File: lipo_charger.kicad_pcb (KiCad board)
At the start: 2 copper layers, 32.3 x 25.4 mm, 19 parts, among them J1 USB_B_Micro, J2 Header, Q1 2N7002DW-7-F, SW1 SW_SPDT, U1 MCP73831, U2 DIO6605B, U3 AP9101CK

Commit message: Finish routing and generate gerbers
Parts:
- added G***: LOGO, LOGO, B.Cu at (149.0, 114.9)
- moved J2 3.87 mm to (135.4, 104.1)
- moved SW1 2.70 mm to (150.1, 104.1)
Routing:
- net GND: track 0.00 -> 50.1 mm, vias 0 -> 5
- net Net-(Q1-Pad5): track 0.00 -> 10.8 mm
- net Net-(SW1-Pad3): track 25.7 -> 21.2 mm, vias 0 -> 1
- net +5V: track 15.3 -> 19.6 mm
- net +BATT: track 50.4 -> 52.2 mm
- net Net-(Q1-Pad2): track 12.8 -> 12.1 mm
- net Net-(L1-Pad1): track 3.39 -> 4.04 mm
- added copper zone on B.Cu, net GND
- removed copper zone on F.Cu, net GND
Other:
- board text added: "+"
- board text added: "-"
- board text added: "5V"
- board text added: "Noah White"
- board text added: "Rev 1.0"

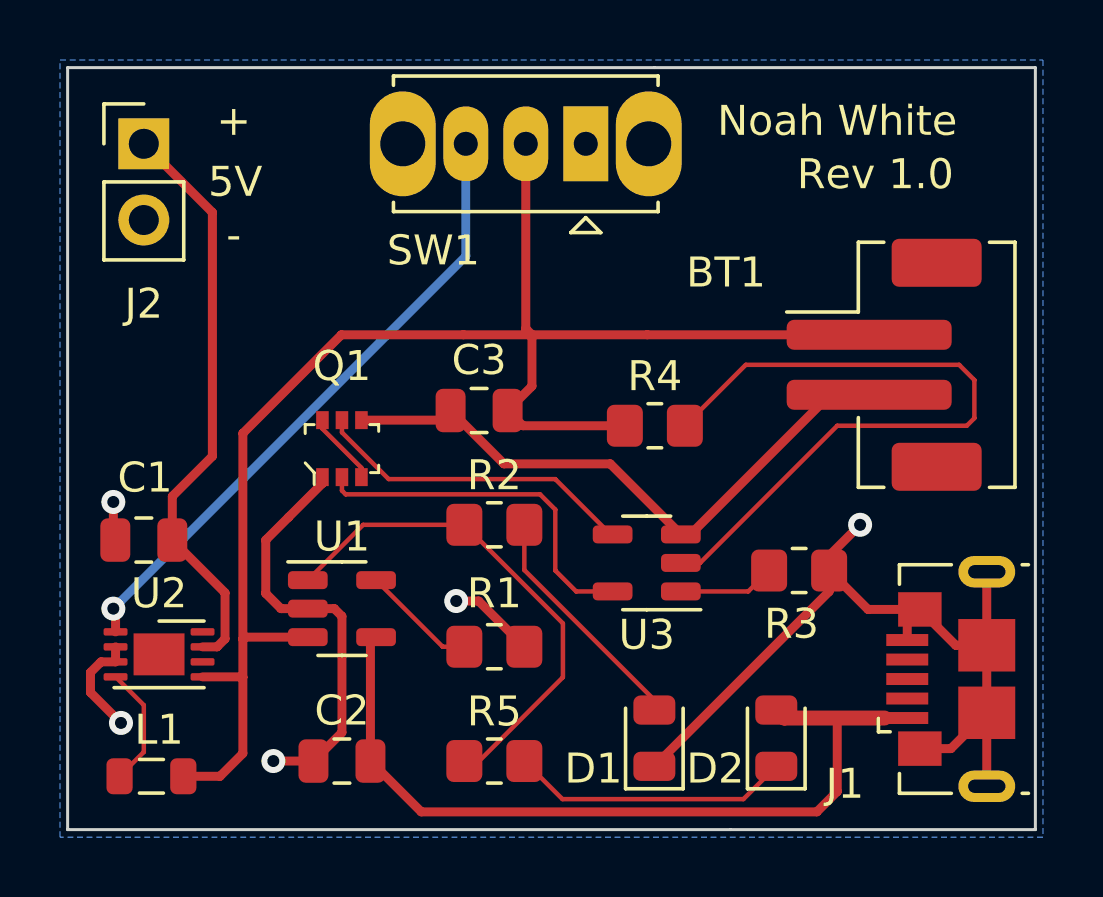
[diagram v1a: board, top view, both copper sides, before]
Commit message: Create footprint for boost IC and reroute
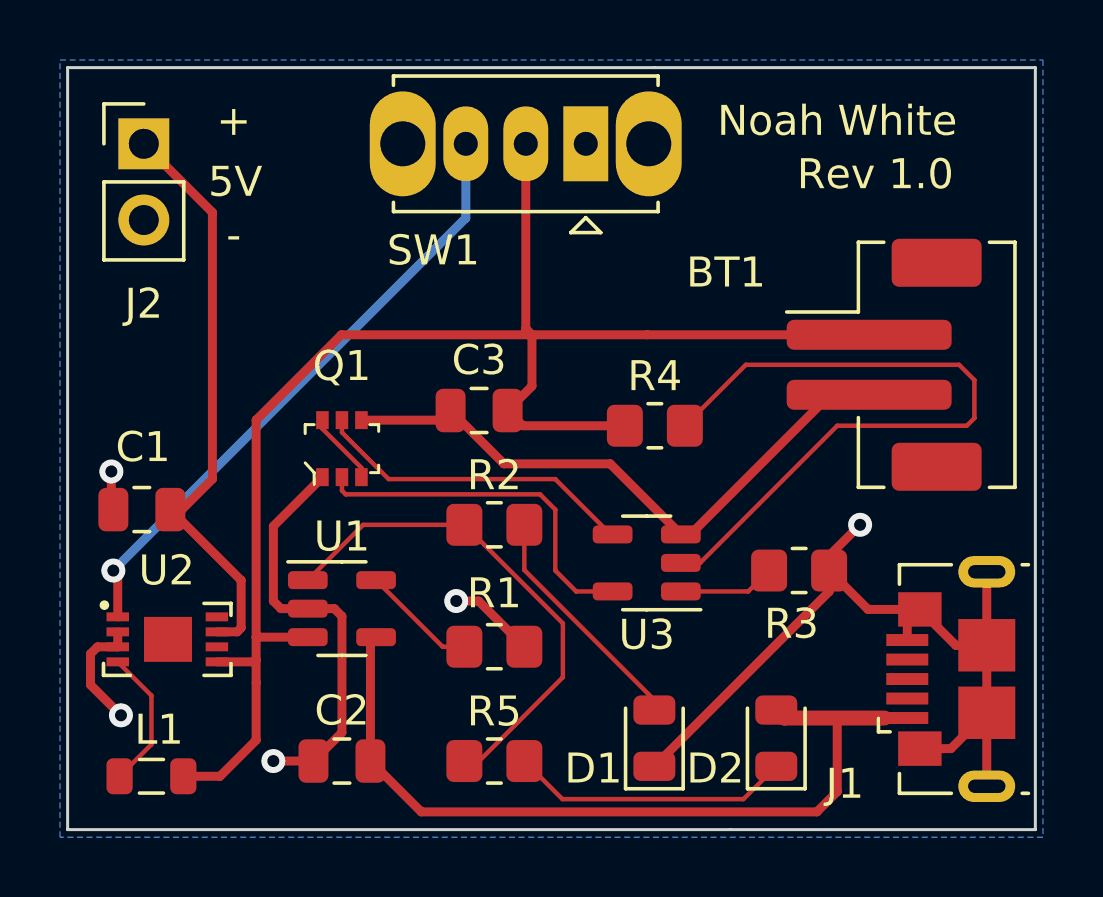
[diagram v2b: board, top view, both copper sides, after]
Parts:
- J2: value Header -> 22-23-2021
- U2: footprint Package_DFN_QFN:DFN-8-1EP_3x2mm_P0.5mm_EP1.7x1.4mm -> Package_DFN_QFN:DFN-8-1EP_3x2mm_P0.5mm_EP1.6x1.5mm
- moved U2 2.35 mm to (137.7, 119.6), turned to -90 degrees
- moved C1 1.02 mm to (135.3, 116.3)
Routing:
- net Net-(L1-Pad1): track 4.04 -> 4.72 mm

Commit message: Reroute PCB with new Q2 footprint
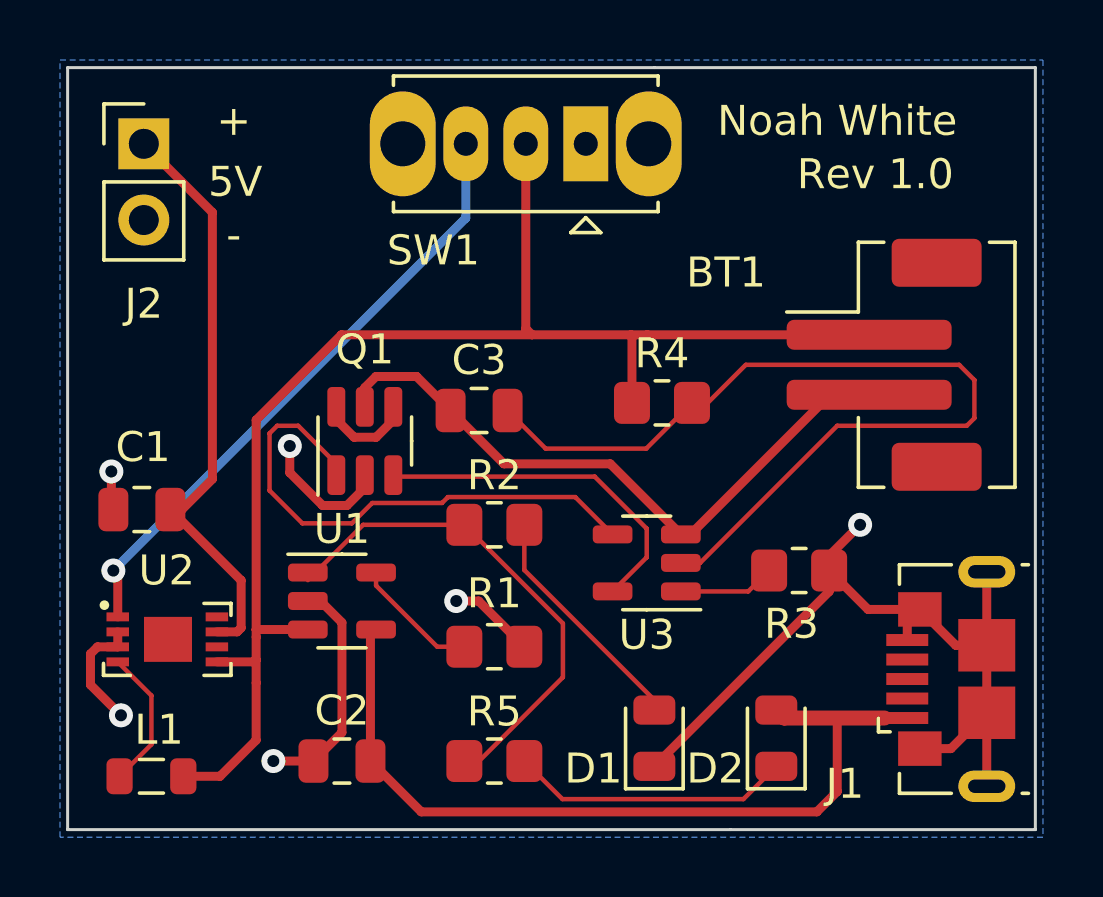
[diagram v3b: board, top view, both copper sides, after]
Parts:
- Q1: value 2N7002DW-7-F -> DMN2053UVT; footprint digikey-footprints:SOT-363 -> Package_TO_SOT_SMD:TSOT-23-6
- R3: value 4.7k -> 1k
- moved Q1 0.80 mm to (142.7, 114.0), turned to 90 degrees
- moved R4 0.80 mm to (152.7, 112.8)
- moved U1 0.25 mm to (142.0, 119.4)
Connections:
- C3 pad 2: +BATT -> Net-(C3-Pad2)
- Q1 pad 1: GND -> Net-(Q1-Pad1)
- Q1 pad 2: Net-(Q1-Pad2) -> GND
- Q1 pad 4: -BATT -> Net-(Q1-Pad4)
- Q1 pad 5: Net-(Q1-Pad5) -> -BATT
- Q1 pad 6: Net-(Q1-Pad3) -> Net-(Q1-Pad4)
- R4 pad 2: Net-(R4-Pad2) -> Net-(C3-Pad2)
- U3 pad 2: Net-(R4-Pad2) -> Net-(C3-Pad2)
- U3 pad 4: Net-(Q1-Pad5) -> Net-(Q1-Pad1)
- U3 pad 5: Net-(Q1-Pad2) -> Net-(Q1-Pad3)
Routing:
- net Net-(C3-Pad2): track 0.00 -> 30.5 mm
- net Net-(R4-Pad2): track 23.8 -> 0.00 mm
- net Net-(Q1-Pad1): track 0.00 -> 17.9 mm
- net Net-(Q1-Pad2): track 12.1 -> 0.00 mm
- net Net-(Q1-Pad5): track 10.8 -> 0.00 mm
- net Net-(Q1-Pad3): track 2.44 -> 11.8 mm
- net +BATT: track 51.7 -> 47.0 mm
- net Net-(Q1-Pad4): track 0.00 -> 3.24 mm
- net GND: track 50.3 -> 48.7 mm, vias 5 -> 6
- net -BATT: track 20.7 -> 21.7 mm

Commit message: Replace switch and reroute
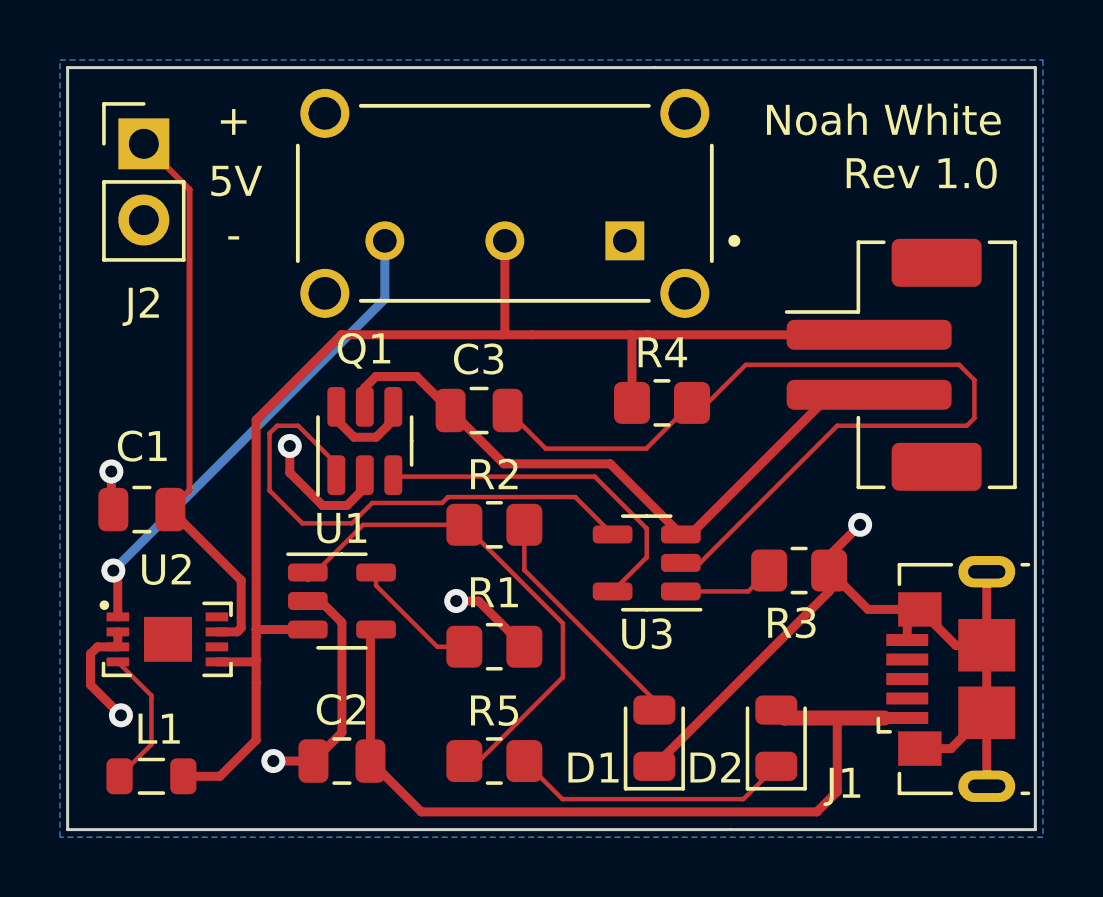
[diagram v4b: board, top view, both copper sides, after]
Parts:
- SW1: footprint Button_Switch_THT:SW_Slide_1P2T_CK_OS102011MS2Q -> footprint_libs:SW_EG1224
- moved SW1 3.35 mm to (147.4, 106.1)
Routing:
- net Net-(SW1-Pad3): track 20.7 -> 16.3 mm
- net +BATT: track 47.0 -> 43.7 mm
- net +5V: track 19.7 -> 18.9 mm

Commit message: Replace switch footprint on PCB
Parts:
- SW1: footprint footprint_libs:SW_EG1224 -> Button_Switch_THT:SW_CuK_OS102011MA1QN1_SPDT_Angled
- moved SW1 2.91 mm to (149.5, 104.1)
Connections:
- SW1 pad 1: unconnected-(SW1-Pad1) -> Net-(SW1-Pad1)
- SW1 pad 2: +BATT -> Net-(Q1-Pad1)
- SW1 pad 3: Net-(SW1-Pad3) -> -BATT
- U2 pad 1: Net-(SW1-Pad3) -> +BATT
- U3 pad 4: Net-(Q1-Pad1) -> Net-(SW1-Pad1)
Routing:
- net Net-(SW1-Pad3): track 16.3 -> 0.00 mm, vias 1 -> 0
- net +BATT: track 43.7 -> 42.3 mm, vias 0 -> 1

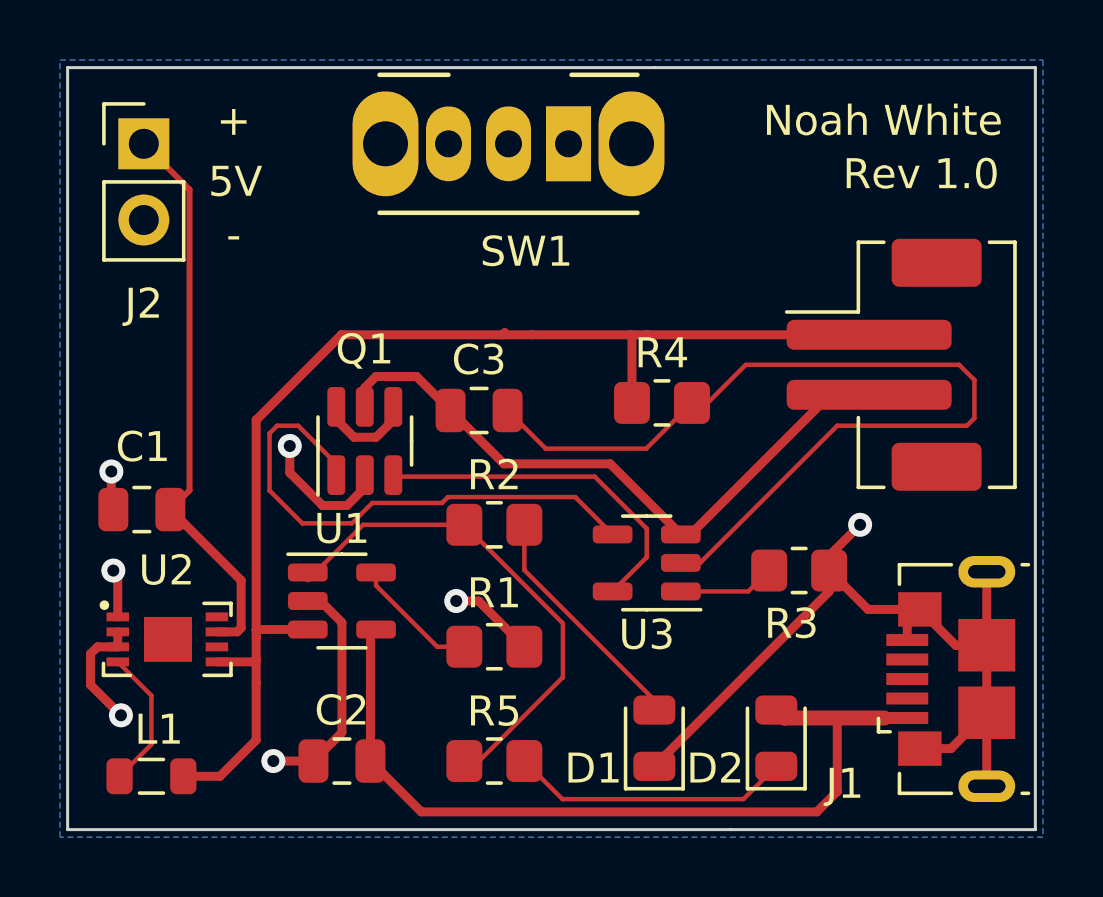
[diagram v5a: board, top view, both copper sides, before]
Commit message: Completely reroute PCB
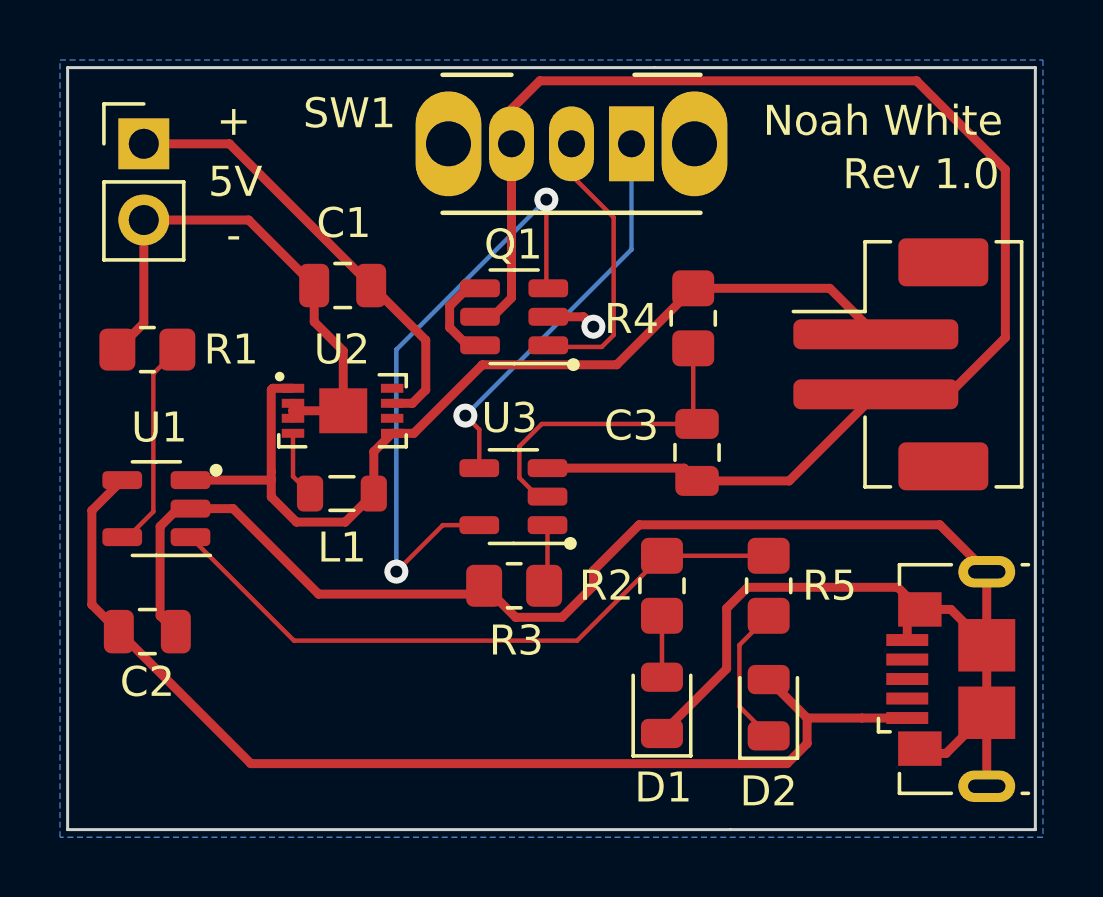
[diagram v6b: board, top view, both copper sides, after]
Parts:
- moved R1 15.2 mm to (135.5, 111.0), turned to 0 degrees
- moved L1 11.4 mm to (142.0, 115.8)
- moved R5 10.9 mm to (156.2, 118.9), turned to -90 degrees
- moved C1 10.0 mm to (142.0, 108.9)
- moved U2 9.60 mm to (143.5, 112.0)
- moved R3 9.51 mm to (147.7, 118.9), turned to 0 degrees
- moved C2 7.79 mm to (135.5, 120.4), turned to 180 degrees
- moved C3 7.40 mm to (153.8, 114.4), turned to 90 degrees
- moved U1 6.91 mm to (135.8, 116.3), turned to 180 degrees
- moved Q1 6.48 mm to (147.7, 109.9), turned to 180 degrees
- moved R2 5.95 mm to (152.7, 118.9), turned to -90 degrees
- moved U3 4.96 mm to (147.7, 115.9)
- moved R4 3.01 mm to (153.7, 110.0), turned to -90 degrees
- moved SW1 2.10 mm to (151.6, 104.1)
- moved D1 1.12 mm to (152.7, 122.9)
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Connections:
- U2 pad 9: (no net) -> GND
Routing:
- net GND: track 48.7 -> 81.2 mm, vias 6 -> 1
- net -BATT: track 21.7 -> 48.7 mm
- net Net-(C3-Pad2): track 30.5 -> 11.1 mm
- net Net-(SW1-Pad1): track 0.00 -> 13.3 mm, vias 0 -> 1
- net +BATT: track 42.3 -> 32.2 mm, vias 1 -> 0
- net VBUS: track 27.0 -> 36.9 mm
- net Net-(Q1-Pad3): track 11.8 -> 20.9 mm, vias 0 -> 2
- net Net-(Q1-Pad1): track 17.9 -> 9.32 mm
- net Net-(D1-Pad2): track 7.97 -> 2.05 mm
- net Net-(R2-Pad1): track 16.9 -> 21.9 mm
- net Net-(D2-Pad1): track 9.38 -> 4.81 mm
- net +5V: track 18.9 -> 15.1 mm
- net Net-(R1-Pad2): track 4.22 -> 7.12 mm
- net Net-(L1-Pad1): track 4.72 -> 2.25 mm
- net Net-(R3-Pad2): track 3.23 -> 2.07 mm
